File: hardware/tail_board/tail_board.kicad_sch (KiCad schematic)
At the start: 18 parts, among them J1 DC IN, J2 DC THRU, J3 Head, J4 Camera, J5 8P8C_Shielded, Q1 DMP3037LSS-13

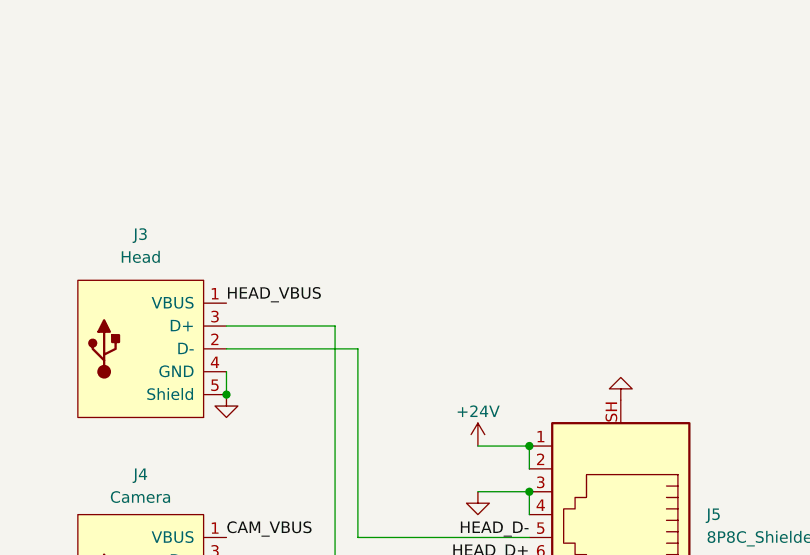
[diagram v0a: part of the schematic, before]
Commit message: Add smart solenoid drivers
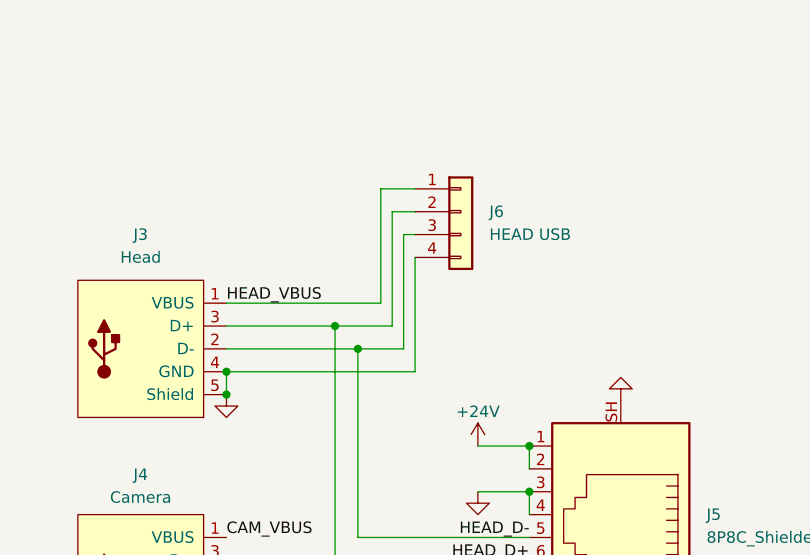
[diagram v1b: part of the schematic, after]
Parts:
- added J6: HEAD USB, Connector_JST:JST_XH_B4B-XH-A_1x04_P2.50mm_Vertical, symbol Connector_Generic:Conn_01x04
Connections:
- net GND: now also J6.4 (Pin_4)
- net HEAD_D+: now also J6.2 (Pin_2)
- net HEAD_D-: now also J6.3 (Pin_3)
- net HEAD_VBUS: now also J6.1 (Pin_1)
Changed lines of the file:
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@@
   (junction (at 77.47 44.45) (diameter 0) (color 0 0 0 0)
   )
+  (junction (at 182.88 55.88) (diameter 0) (color 0 0 0 0)
+  )
+  (junction (at 194.945 50.8) (diameter 0) (color 0 0 0 0)
+  )
   (junction (at 129.54 194.945) (diameter 0) (color 0 0 0 0)
   )
@@
   (junction (at 216.535 64.135) (diameter 0) (color 0 0 0 0)
   )
+  (junction (at 197.485 53.34) (diameter 0) (color 0 0 0 0)
+  )
   (junction (at 182.88 58.42) (diameter 0) (color 0 0 0 0)
   )
@@
     (stroke (width 0) (type default) (color 0 0 0 0))
   )
+  (wire (pts (xy 201.295 38.1) (xy 203.835 38.1))
+    (stroke (width 0) (type default) (color 0 0 0 0))
+  )
   (wire (pts (xy 216.535 64.135) (xy 216.535 66.675))
     (stroke (width 0) (type default) (color 0 0 0 0))
@@
     (stroke (width 0) (type default) (color 0 0 0 0))
   )
+  (wire (pts (xy 202.565 53.34) (xy 202.565 40.64))
+    (stroke (width 0) (type default) (color 0 0 0 0))
+  )
   (wire (pts (xy 105.41 41.91) (xy 105.41 44.45))
     (stroke (width 0) (type default) (color 0 0 0 0))
@@
     (stroke (width 0) (type default) (color 0 0 0 0))
   )
+  (wire (pts (xy 203.835 55.88) (xy 203.835 43.18))
+    (stroke (width 0) (type default) (color 0 0 0 0))
+  )
+  (wire (pts (xy 202.565 40.64) (xy 203.835 40.64))
+    (stroke (width 0) (type default) (color 0 0 0 0))
+  )
+  (wire (pts (xy 194.945 50.8) (xy 201.295 50.8))
+    (stroke (width 0) (type default) (color 0 0 0 0))
+  )
+  (wire (pts (xy 201.295 50.8) (xy 201.295 38.1))
+    (stroke (width 0) (type default) (color 0 0 0 0))
+  )
   (wire (pts (xy 134.62 194.945) (xy 139.065 194.945))
     (stroke (width 0) (type default) (color 0 0 0 0))
   )
+  (wire (pts (xy 182.88 48.26) (xy 200.025 48.26))
+    (stroke (width 0) (type default) (color 0 0 0 0))
+  )
   (wire (pts (xy 187.325 76.835) (xy 182.88 76.835))
     (stroke (width 0) (type default) (color 0 0 0 0))
@@
     (stroke (width 0) (type default) (color 0 0 0 0))
   )
+  (wire (pts (xy 200.025 35.56) (xy 203.835 35.56))
+    (stroke (width 0) (type default) (color 0 0 0 0))
+  )
   (wire (pts (xy 100.33 31.75) (xy 105.41 31.75))
     (stroke (width 0) (type default) (color 0 0 0 0))
@@
     (stroke (width 0) (type default) (color 0 0 0 0))
   )
+  (wire (pts (xy 182.88 55.88) (xy 203.835 55.88))
+    (stroke (width 0) (type default) (color 0 0 0 0))
+  )
   (wire (pts (xy 194.945 76.835) (xy 194.945 50.8))
     (stroke (width 0) (type default) (color 0 0 0 0))
@@
   )
   (wire (pts (xy 139.065 191.77) (xy 139.065 194.945))
+    (stroke (width 0) (type default) (color 0 0 0 0))
+  )
+  (wire (pts (xy 200.025 48.26) (xy 200.025 35.56))
+    (stroke (width 0) (type default) (color 0 0 0 0))
+  )
+  (wire (pts (xy 197.485 53.34) (xy 202.565 53.34))
     (stroke (width 0) (type default) (color 0 0 0 0))
   )
@@
     (pin "1")
   )
+  (symbol (lib_id "Connector_Generic:Conn_01x04") (at 208.915 38.1 0) (unit 1)
+    (in_bom yes) (on_board yes) (fields_autoplaced)
+    (property "Reference" "J6" (id 0) (at 212.09 38.0999 0)
+      (effects (font (size 1.27 1.27)) (justify left))
+    )
+    (property "Value" "HEAD USB" (id 1) (at 212.09 40.6399 0)
+      (effects (font (size 1.27 1.27)) (justify left))
+    )
+    (property "Footprint" "Connector_JST:JST_XH_B4B-XH-A_1x04_P2.50mm_Vertical" (id 2) (at 208.915 38.1 0)
+      (effects (font (size 1.27 1.27)) hide)
+    )
+    (property "Datasheet" "~" (id 3) (at 208.915 38.1 0)
+      (effects (font (size 1.27 1.27)) hide)
+    )
+    (pin "1")
+    (pin "2")
+    (pin "3")
+    (pin "4")
+  )
   (symbol (lib_id "power:GND") (at 128.905 83.82 0) (unit 1)
     (in_bom yes) (on_board yes) (fields_autoplaced)
@@
       (reference "J5") (unit 1) (value "8P8C_Shielded") (footprint "winterbloom:Connector_RJ45_SS-7188S-A-PG4-BA-50")
     )
+    (path "/7440f912-54d5-4395-8d15-4497d066fcd9"
+      (reference "J6") (unit 1) (value "HEAD USB") (footprint "Connector_JST:JST_XH_B4B-XH-A_1x04_P2.50mm_Vertical")
+    )
     (path "/fdf086a4-e118-4324-a2b4-36fbeb364890"

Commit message: V1 of the tailboard
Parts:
- removed J6: HEAD USB, Connector_JST:JST_XH_B4B-XH-A_1x04_P2.50mm_Vertical, symbol Connector_Generic:Conn_01x04
- added C2, C3: 100u, Capacitor_SMD:CP_Elec_6.3x9.9, symbol Device:C_Polarized_US
- added J6: Bottom camera, winterbloom:USB_B_Receptacle_Horizontal, symbol winterbloom:USB_B_Receptacle
- added J7: Bottom camera, Connector_JST:JST_SH_SM04B-SRSS-TB_1x04-1MP_P1.00mm_Horizontal, symbol Connector_Generic_MountingPin:Conn_01x04_MountingPin
- J1, J2: footprint winterbloom:TerminalBlock_4UCON_1x02_P3.50mm_Horizontal -> winterbloom:TerminalBlock_CUI_TB002-500_1x02_P5.00mm_Vertical; mpn (none) -> TB002-500-02BE
- J3: footprint Connector_USB:USB_B_Lumberg_2411_02_Horizontal -> winterbloom:USB_B_Receptacle_Horizontal
- J4: value Camera -> Top camera; footprint Connector_USB:USB_B_Lumberg_2411_02_Horizontal -> winterbloom:USB_B_Receptacle_Horizontal
- R1, R2, R3: footprint Resistor_SMD:R_0603_1608Metric_Pad0.98x0.95mm_HandSolder -> winterbloom:R_0402_HandSolder
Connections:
- net +24V: now also J5.6, J5.8, C2.1, C3.1; no longer J5.1, J5.2
- net CAM_D+: now also J5.1; no longer J5.8
- net CAM_D-: now also J5.2; no longer J5.7
- net GND: now also J5.7, C2.2, C3.2; no longer H1.1, H2.1, J5.4
- net HEAD_D+: now also J5.4; no longer J5.6
- new net: J6.1 (VBUS), J7.1 (Pin_1)
- new net: J6.4 (GND), J6.5 (Shield), J7.4 (Pin_4), J7.MP (MountPin)
- new net BTM_CAM_D+: J6.3 (D+), J7.3 (Pin_3)
- new net BTM_CAM_D-: J6.2 (D-), J7.2 (Pin_2)
- no-connect marks 0 -> 2
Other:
- note added: "TODO: Use CUI footprint"
- title: Candela tail -> Jellyfish Tailboard
- moved on the sheet: C1, D1, D2, D3, J3, J4, R1, R2, R3
